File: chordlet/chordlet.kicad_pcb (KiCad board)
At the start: 2 copper layers, 15 parts, among them J1 Conn_01x06_Socket, J2 Conn_01x06_Socket, J3 Conn_01x01_Pin, SW0 SW_Push, SW1 SW_Push, SW2 SW_Push, SW3 SW_Push, SW4 SW_Push, SW5 SW_DPDT_x2, U1 MCP23008-xSS

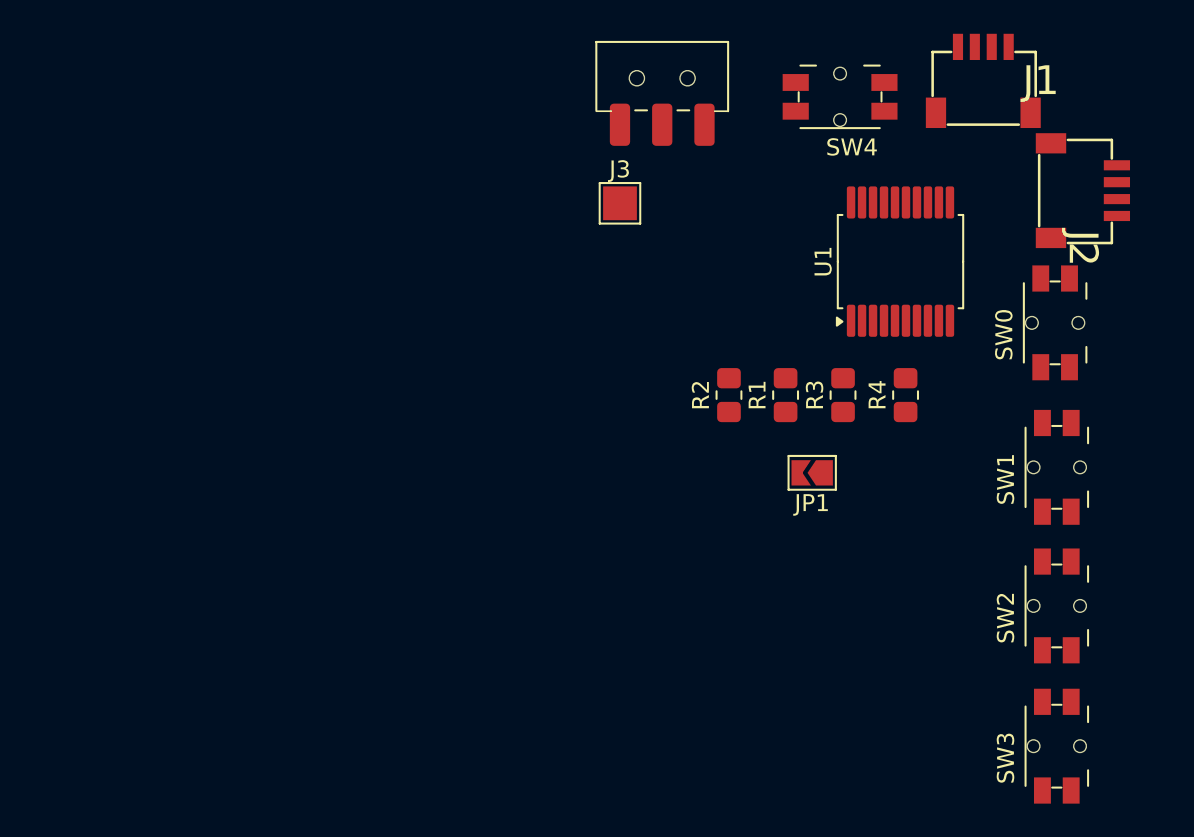
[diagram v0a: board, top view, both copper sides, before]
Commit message: pcb laid out
looks workable, one vcc jumper needed.
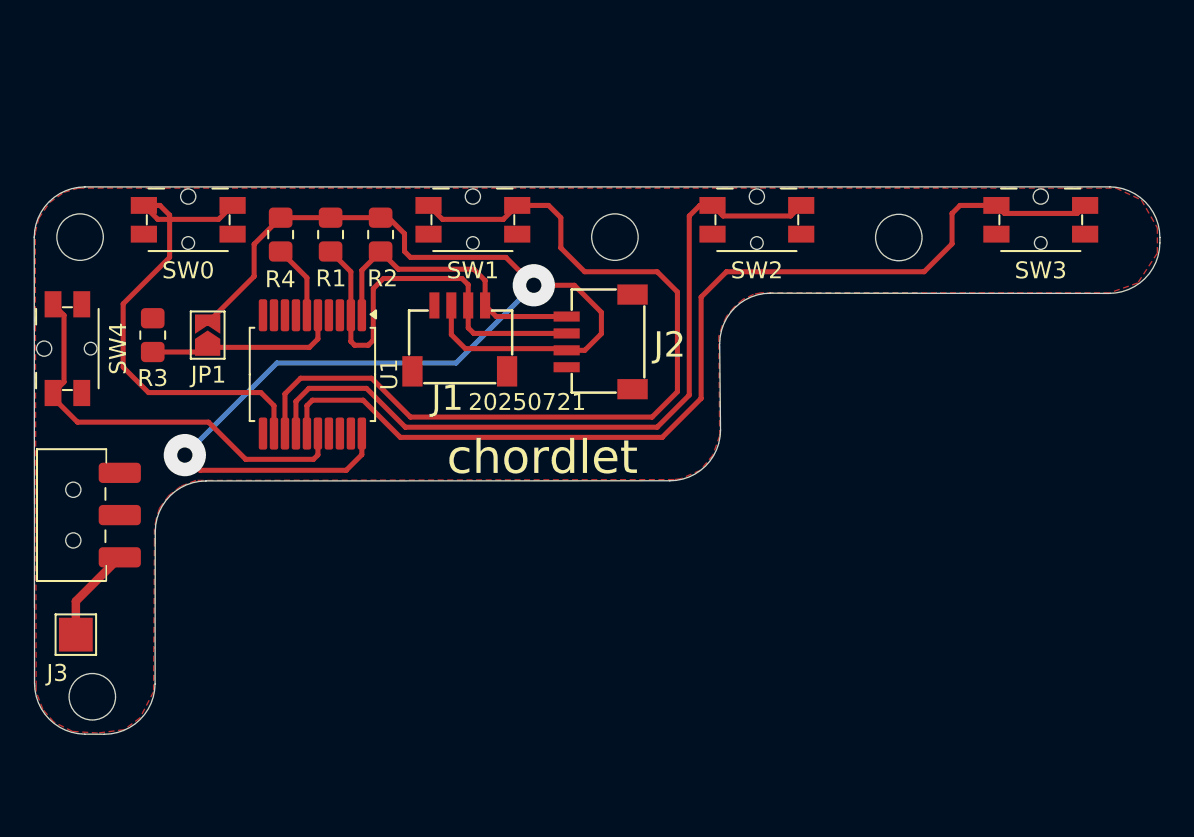
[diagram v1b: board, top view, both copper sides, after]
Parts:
- moved SW0 51.7 mm to (196.8, 84.5), turned to 0 degrees
- moved SW4 48.1 mm to (189.7, 92.2), turned to 90 degrees
- moved SW5 43.0 mm to (190.3, 102.0), turned to -90 degrees
- moved J3 41.1 mm to (190.2, 109.1), turned to -90 degrees
- moved R3 41.0 mm to (194.8, 91.3), turned to -90 degrees
- moved R4 38.2 mm to (202.3, 85.4), turned to -90 degrees
- moved SW1 37.5 mm to (213.7, 84.5), turned to 0 degrees
- moved JP1 36.7 mm to (198.0, 91.3), turned to 90 degrees
- moved U1 35.4 mm to (204.2, 93.7), turned to -90 degrees
- moved J1 34.6 mm to (212.9, 91.6)
- moved SW3 31.2 mm to (247.3, 84.5), turned to 0 degrees
- moved J2 29.9 mm to (221.2, 91.8), turned to 90 degrees
- moved SW2 28.9 mm to (230.5, 84.5), turned to 0 degrees
- moved R1 28.6 mm to (205.3, 85.4), turned to -90 degrees
- moved R2 22.7 mm to (208.2, 85.4), turned to -90 degrees
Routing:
- net VCC: track 0.00 -> 80.2 mm, vias 0 -> 2
- net /pinky: track 0.00 -> 59.4 mm
- net /middle: track 0.00 -> 52.0 mm
- net /ring: track 0.00 -> 45.8 mm
- net /index: track 0.00 -> 29.4 mm
- net /SDA: track 0.00 -> 24.9 mm
- net /thumb: track 0.00 -> 24.6 mm
- net /SCL: track 0.00 -> 17.7 mm
- net /A0: track 0.00 -> 11.5 mm
- net Net-(J3-Pin_1): track 0.00 -> 5.65 mm
- net Net-(U1-~{RESET}): track 0.00 -> 4.42 mm
- added copper zone on F.Cu, net GND
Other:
- board outline added: 66.6 x 32.4 mm
- board text added: "20250721"
- board text added: "chordlet"
